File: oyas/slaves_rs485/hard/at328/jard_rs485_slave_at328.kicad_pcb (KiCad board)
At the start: 2 copper layers, 79.2 x 30 mm, 59 parts, among them J1 EV1, J2 Niveaux, J3 POWER, J4 Débit, J5 Prog MSP, Q1 BPC_FMMT38C, Q2 P03P4L-04, U1 BPC_Alim3_3V, U2 MSP430F1232IDW, U3 MAX485E, Y1 8MHz

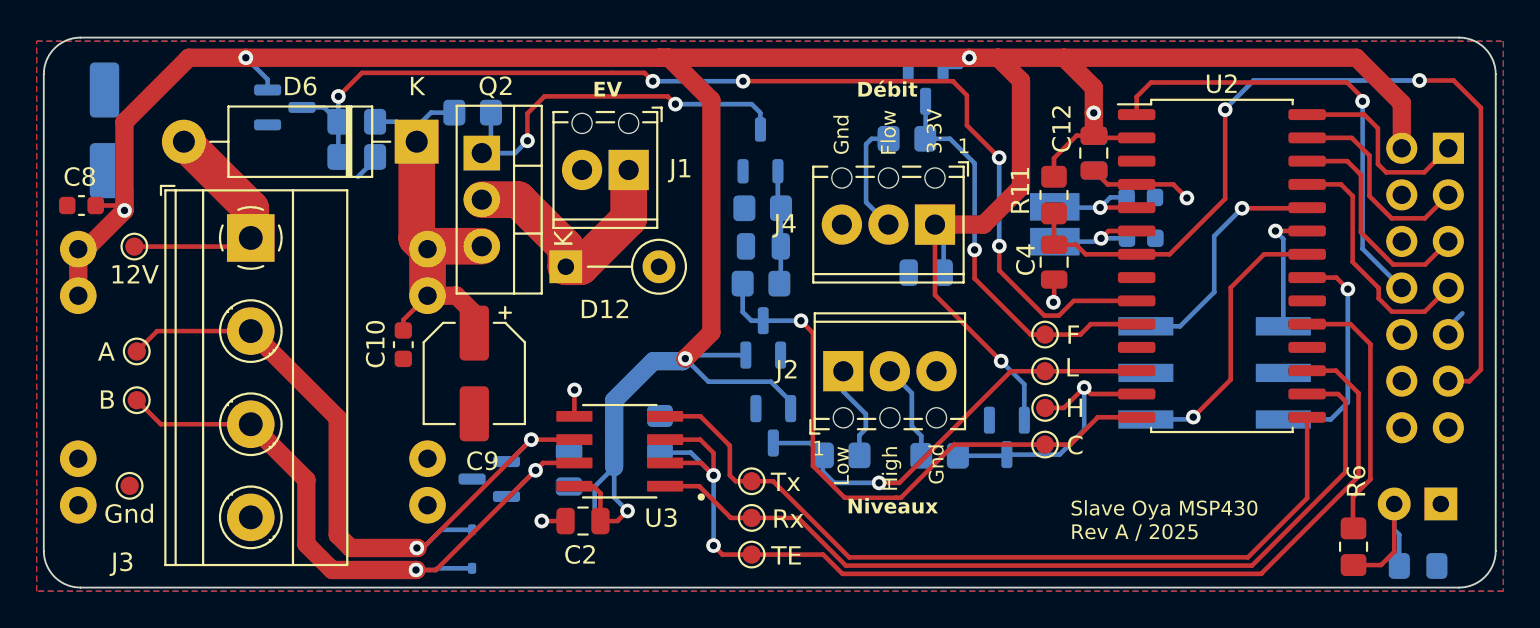
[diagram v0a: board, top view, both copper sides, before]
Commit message: Creation carte esclave à base de AT328 (à finir - Connecter power 12V mes, ...)
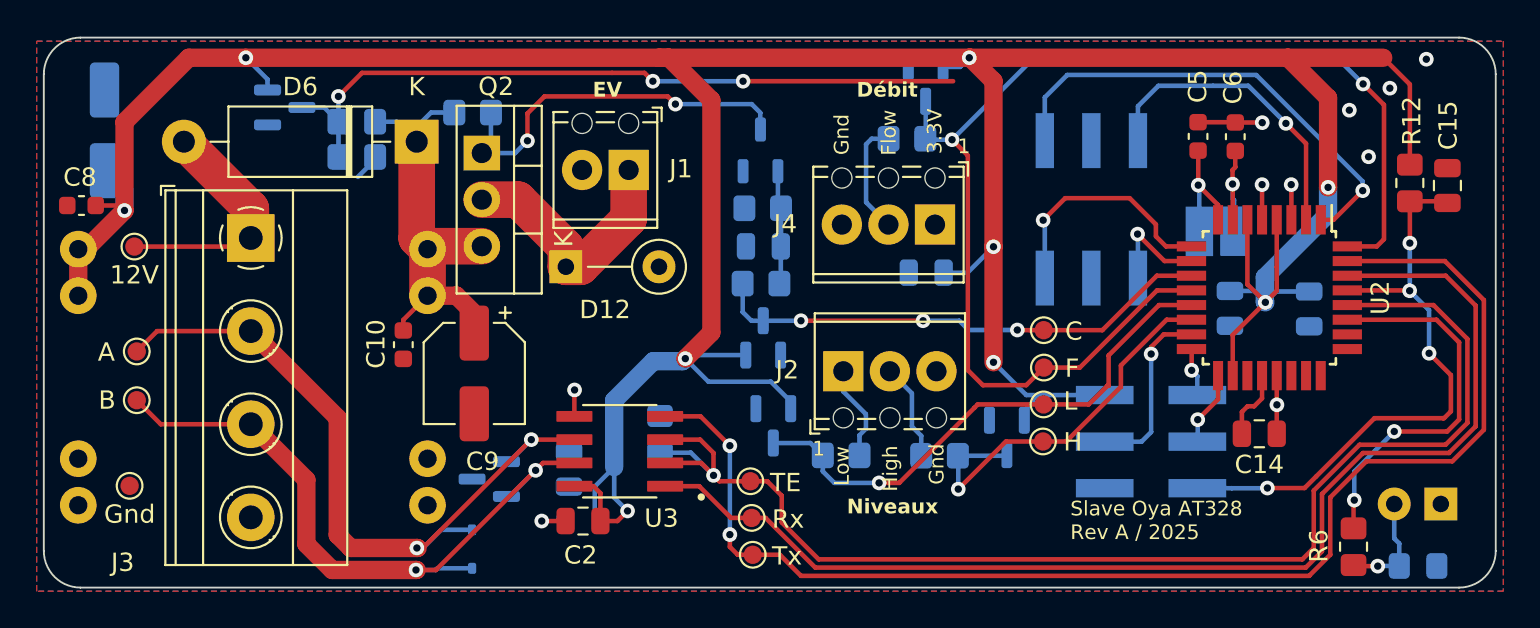
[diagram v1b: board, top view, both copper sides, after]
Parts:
- removed C4: 1nF, Capacitor_SMD:C_0805_2012Metric
- removed R11: 100k, Resistor_SMD:R_0805_2012Metric_Pad1.20x1.40mm_HandSolder
- added C14: 100nF, Capacitor_SMD:C_0805_2012Metric, F.Cu at (179.7, 108.4)
- added C15: 100nF, Capacitor_SMD:C_0805_2012Metric, F.Cu at (189.9, 94.9)
- added R12: 100, Resistor_SMD:R_0805_2012Metric_Pad1.20x1.40mm_HandSolder, F.Cu at (187.9, 94.7)
- C12: moved to B.Cu
- C5, C6: moved to F.Cu
- J5: value Prog MSP -> ISCP; footprint bpc:BPC_PROG_MSP -> bpc:BPC_ISCP_CMS
- U1: value BPC_Alim3_3V -> BPC_Alim5V; footprint bpc:BPC_Alim3_3V -> bpc:BPC_Alim5V
- U2: value MSP430F1232IDW -> ATmega328P-A; footprint Package_SO:SOIC-28W_7.5x17.9mm_P1.27mm -> Package_QFP:TQFP-32_7x7mm_P0.8mm
- moved J5 22.8 mm to (173.8, 108.8)
- moved C12 14.5 mm to (182.4, 101.6), turned to -90 degrees
- moved C11 11.2 mm to (178.1, 101.6), turned to -90 degrees
- moved S1 11.2 mm to (170.5, 96.2), turned to -90 degrees
- moved Y1 8.83 mm to (177.4, 97.4), turned to 0 degrees
- moved C5 6.37 mm to (176.3, 92.2), turned to 90 degrees
- moved TP11 6.24 mm to (167.9, 102.8)
- moved C6 6.13 mm to (178.4, 92.2), turned to -90 degrees
- moved TP4 4.01 mm to (152.1, 115.0)
- moved TP5 4.00 mm to (151.9, 111.0)
- moved U2 3.12 mm to (180.2, 101.0), turned to -90 degrees
- moved TP1 1.83 mm to (167.9, 108.8)
- moved TP2 1.81 mm to (167.9, 106.8)
- moved TP10 1.80 mm to (167.9, 104.8)
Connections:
- C1 pad 1: +3.3V -> +5V
- C11 pad 1: GND -> +5V
- C11 pad 2: +3.3V -> GND
- C12 pad 1: GND -> +5V
- C12 pad 2: +3.3V -> GND
- C13 pad 1: +3.3V -> +5V
- C2 pad 2: +3.3V -> +5V
- C5 pad 1: GND -> Net-(U2-XTAL2/PB7)
- C5 pad 2: Net-(U2-XIN) -> GND
- C6 pad 2: Net-(U2-XOUT) -> Net-(U2-XTAL1/PB6)
- C7 pad 1: +3.3V -> +5V
- C8 pad 1: +3.3V -> +5V
- D1 pad 2: +3.3V -> +5V
- D10 pad 2: +3.3V -> +5V
- D11 pad 2: +3.3V -> +5V
- D2 pad 2: +3.3V -> +5V
- D3 pad 1: +3.3V -> +5V
- D7 pad 2: +3.3V -> +5V
- J5 pad 1: TDO -> MISO
- J5 pad 2: +3.3V -> +5V
- J5 pad 3: TDI -> SCK
- J5 pad 4: unconnected-(J5-Sense-Pad4) -> MOSI
- J5 pad 5: TMS -> RESET
- J5 pad 6: unconnected-(J5-TCLK-Pad6) -> GND
- U1 pad 7: +3.3V -> +5V
- U1 pad 8: +3.3V -> +5V
- U2 pad 1: TEST -> A1
- U2 pad 10: FLOW -> A2
- U2 pad 11: unconnected-(U2-P3.0/A5/STE0-Pad11) -> CMD_EV1
- U2 pad 12: LVL_LOW -> FLOW
- U2 pad 13: LVL_HIGH -> LVL_LOW
- U2 pad 14: CMD_EV1 -> LVL_HIGH
- U2 pad 15: TX -> MOSI
- U2 pad 16: RX -> MISO
- U2 pad 17: TX_EN -> SCK
- U2 pad 18: unconnected-(U2-P3.7/A7-Pad18) -> +5V
- U2 pad 19: LED -> unconnected-(U2-ADC6-Pad19)
- U2 pad 2: +3.3V -> A3
- U2 pad 20: unconnected-(U2-TA2/VeREF+/VREF+/A4/P2.4-Pad20) -> Net-(U2-AREF)
- U2 pad 21: A4 -> GND
- U2 pad 22: A1 -> unconnected-(U2-ADC7-Pad22)
- U2 pad 23: A2 -> unconnected-(U2-PC0-Pad23)
- U2 pad 24: A3 -> unconnected-(U2-PC1-Pad24)
- U2 pad 25: TCK -> unconnected-(U2-PC2-Pad25)
- U2 pad 26: TMS -> unconnected-(U2-PC3-Pad26)
- U2 pad 27: TDI -> LED
- U2 pad 28: TDO -> TX_EN
- U2 pad 3: unconnected-(U2-Rosc/P2.5-Pad3) -> GND
- U2 pad 4: GND -> +5V
- U2 pad 5: Net-(U2-XOUT) -> GND
- U2 pad 6: Net-(U2-XIN) -> +5V
- U2 pad 7: Net-(J5-RST) -> Net-(U2-XTAL1/PB6)
- U2 pad 8: unconnected-(U2-ACLK/A0/P2.0-Pad8) -> Net-(U2-XTAL2/PB7)
- U2 pad 9: POW_MES -> A4
- U3 pad 8: +3.3V -> +5V
- Y1 pad 1: Net-(U2-XOUT) -> Net-(U2-XTAL2/PB7)
- Y1 pad 2: Net-(U2-XIN) -> Net-(U2-XTAL1/PB6)
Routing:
- net +5V: track 0.00 -> 209.2 mm, vias 0 -> 9
- net +3.3V: track 184.2 -> 0.00 mm, vias 7 -> 0
- net Net-(J5-RST): track 49.0 -> 0.00 mm, vias 2 -> 0
- net FLOW: track 21.9 -> 67.2 mm, vias 1 -> 2
- net RESET: track 0.00 -> 33.5 mm, vias 0 -> 4
- net TX: track 44.9 -> 72.0 mm, vias 0 -> 2
- net TEST: track 25.2 -> 0.00 mm, vias 1 -> 0
- net POW_MES: track 60.1 -> 39.9 mm, vias 5 -> 3
- net RX: track 47.1 -> 65.3 mm
- net TCK: track 13.6 -> 0.00 mm
- net TMS: track 12.4 -> 0.00 mm
- net TDI: track 11.3 -> 0.00 mm
- net TX_EN: track 60.2 -> 71.2 mm, vias 2 -> 1
- net TDO: track 10.7 -> 0.00 mm
- net A1: track 15.5 -> 26.1 mm
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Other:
- board text added: "Prog"
- board text added: "Slave Oya AT328 Rev A / 2025"
- board text removed: "Slave Oya MSP430 Rev A / 2025"

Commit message: Finalisation carte AT328
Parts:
- C5, C6: value 15pF -> 10pF
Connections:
- J4 pad 1: +3.3V -> +5V
- U2 pad 25: unconnected-(U2-PC2-Pad25) -> POW_MES
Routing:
- net POW_MES: track 39.9 -> 94.1 mm, vias 3 -> 5
- net +5V: track 209.2 -> 212.9 mm, vias 9 -> 10

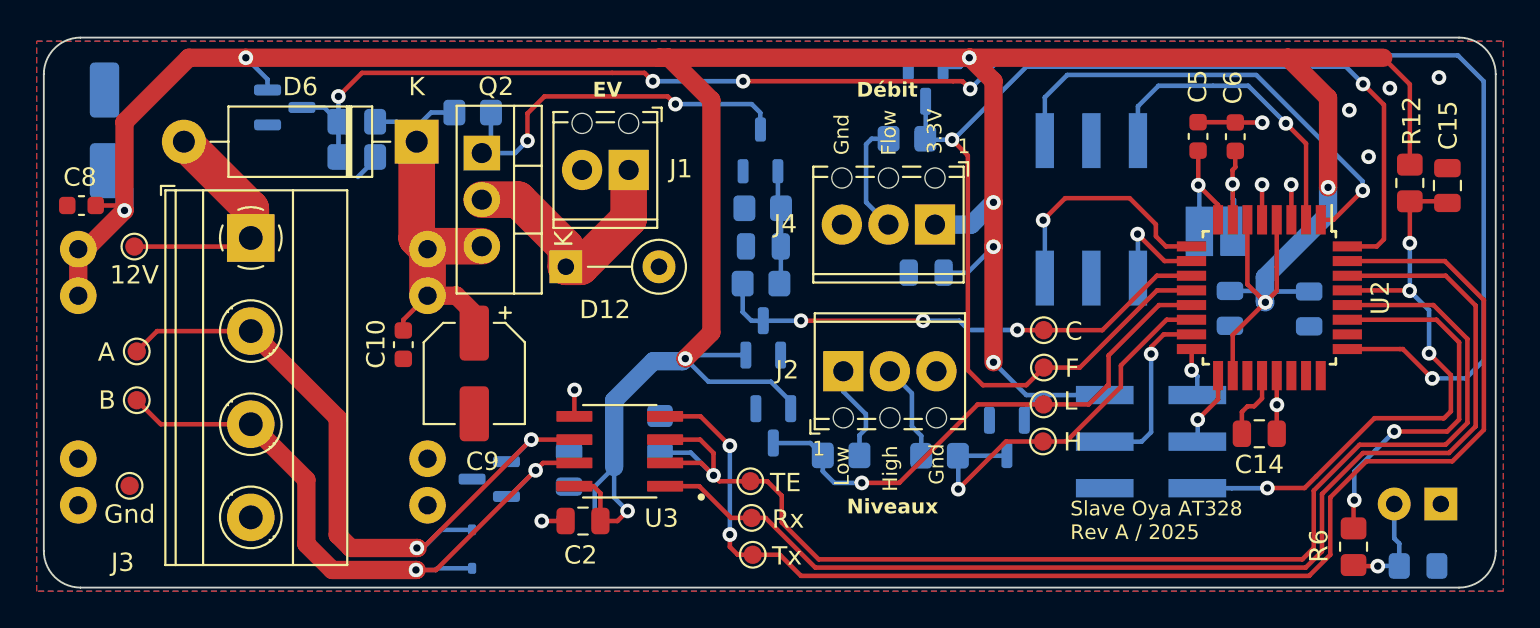
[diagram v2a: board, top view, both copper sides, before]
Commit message: Améliorations sur carte AT328
- Capas en hand soldering et en 805
- TP + gros
- Repères composants
- Carte moins longue
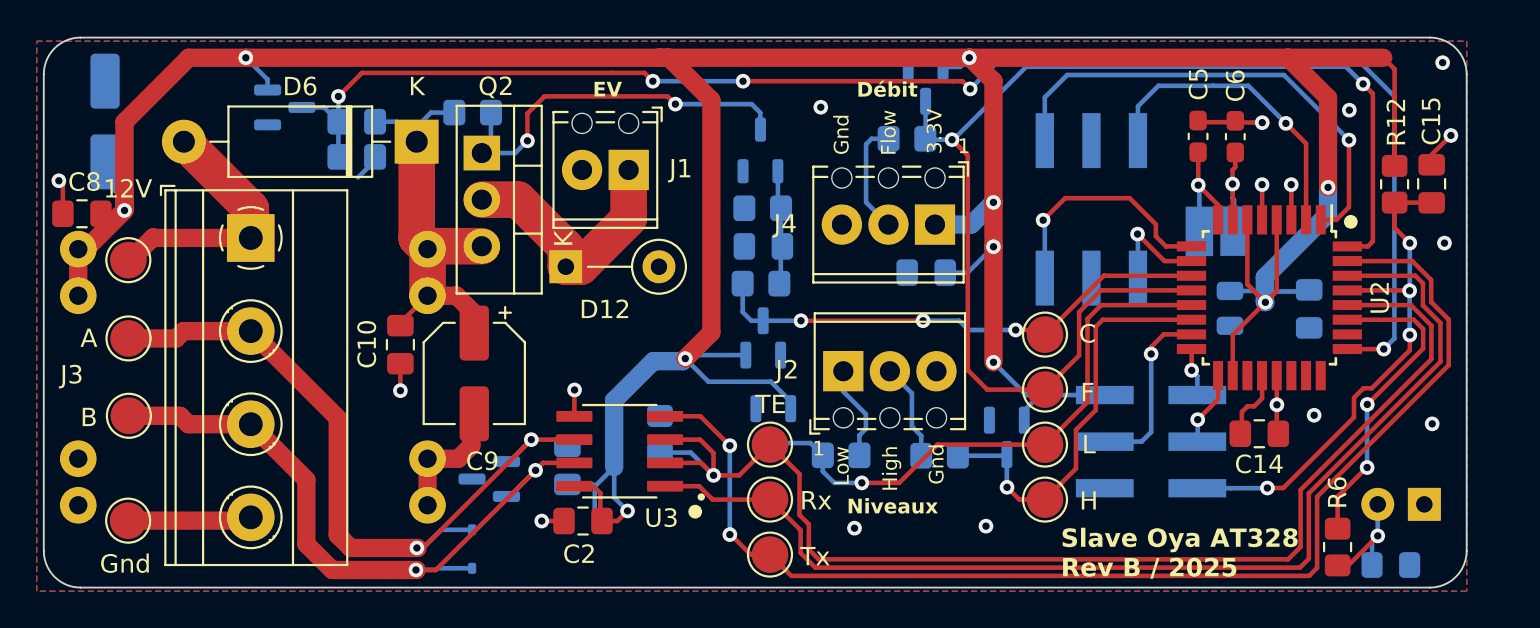
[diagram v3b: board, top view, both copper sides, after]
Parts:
- C1: value 10µF -> 10nF; footprint Capacitor_SMD:C_0805_2012Metric -> Capacitor_SMD:C_0805_2012Metric_Pad1.18x1.45mm_HandSolder
- C10, C8: footprint Capacitor_SMD:C_0603_1608Metric -> Capacitor_SMD:C_0805_2012Metric_Pad1.18x1.45mm_HandSolder
- C12, C13, C14, C15, C2, C3: footprint Capacitor_SMD:C_0805_2012Metric -> Capacitor_SMD:C_0805_2012Metric_Pad1.18x1.45mm_HandSolder
- C5, C6: value 10pF -> 6pF; footprint Capacitor_SMD:C_0603_1608Metric -> Capacitor_SMD:C_0603_1608Metric_Pad1.08x0.95mm_HandSolder
- TP1, TP10, TP11, TP2, TP3, TP4, TP5, TP6, TP7, TP8, TP9: footprint TestPoint:TestPoint_Pad_D1.0mm -> TestPoint:TestPoint_Pad_D2.0mm
- moved TP1 3.17 mm to (168.0, 112.0)
- moved TP5 2.27 mm to (153.0, 109.0)
- moved TP2 2.19 mm to (168.0, 109.0)
- moved TP9 1.90 mm to (118.0, 113.2)
- moved D9 1.48 mm to (186.9, 115.6)
- moved TP3 1.41 mm to (153.0, 112.0)
- moved TP10 1.20 mm to (168.0, 106.0)
- moved TP6 0.95 mm to (118.0, 107.4)
- moved TP4 0.94 mm to (153.0, 115.0)
- moved D8 0.90 mm to (188.7, 112.3)
- moved R6 0.87 mm to (184.0, 114.6)
- moved C15 0.86 mm to (189.1, 94.8)
- moved TP7 0.84 mm to (118.0, 103.2)
- moved R12 0.83 mm to (187.1, 94.8)
- moved TP8 0.81 mm to (118.0, 98.9)
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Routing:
- net GND: track 14.8 -> 34.0 mm, vias 10 -> 17
- net POW_MES: track 94.1 -> 81.8 mm
- net TX: track 72.0 -> 66.3 mm
- net RX: track 65.3 -> 60.6 mm
- net RESET: track 33.5 -> 29.2 mm
- net LED: track 20.8 -> 17.2 mm
- net TX_EN: track 71.2 -> 68.3 mm
- net +5V: track 212.9 -> 211.1 mm
- net LVL_LOW: track 29.2 -> 30.9 mm
- net LVL_HIGH: track 21.8 -> 22.8 mm
- net FLOW: track 66.7 -> 67.5 mm
- net Net-(D6-A): track 13.3 -> 13.9 mm
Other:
- board size 79.2 x 30 mm -> 77.6 x 30 mm
- board text added: "0"
- board text added: "Slave Oya AT328 Rev B / 2025"
- board text removed: "Slave Oya AT328 Rev A / 2025"
